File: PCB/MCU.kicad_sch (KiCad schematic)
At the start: 34 parts, among them J1 SWD, Q1 AO3400A, SW32 USB Boot, SW33 Reset, U2 W25Q128JVS, U3 RP2040, Y1 12MHz

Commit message: More routing
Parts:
- J1: now not fitted
- SW32: footprint Cantaloupe:SW_DIP_SPSTx01_Slide_6.7x4.1mm_W8.61mm_P2.54mm_LowProfile-Dual -> Cantaloupe:SW_DIP_SPSTx01_Slide_6.7x4.1mm_W8.61mm_P2.54mm_LowProfile-Flippable
- SW33: footprint Cantaloupe:SW_SPST_TL3342-Dual -> Cantaloupe:SW_SPST_TL3342-Flippable
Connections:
- net ROTA: now also U3.28 (GPIO17); no longer U3.27 (GPIO16)
- net ROTB: now also U3.29 (GPIO18); no longer U3.28 (GPIO17)
- net ROW4: now also U3.27 (GPIO16); no longer U3.29 (GPIO18)
- net Side: now also U3.14 (GPIO11)
- net RGB_3V3: now reaches Q1.2 (S), R19.1, U3.34 (GPIO22)
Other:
- moved on the sheet: JP1, JP2, Q1, R10, R19, R20

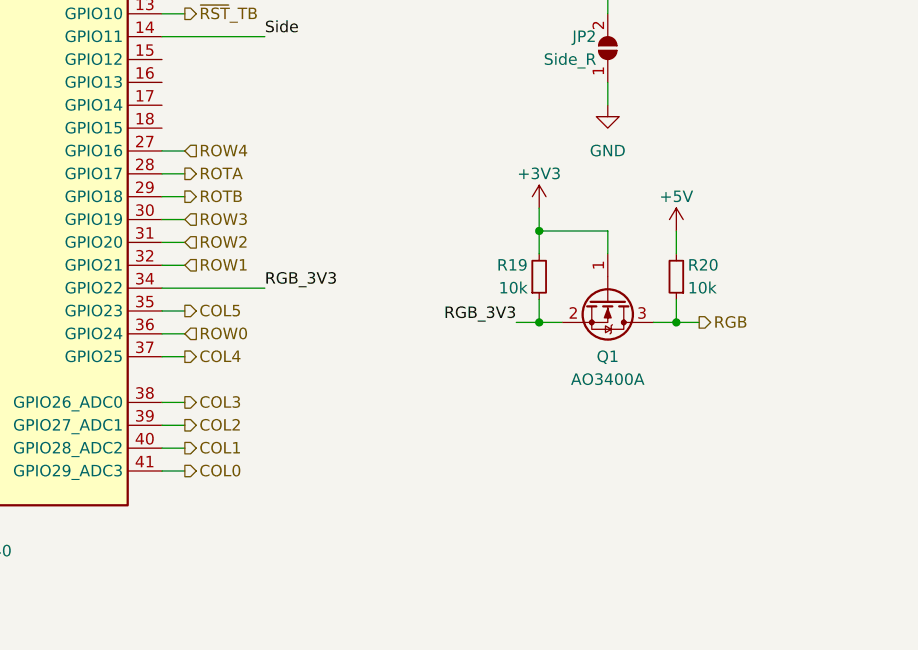
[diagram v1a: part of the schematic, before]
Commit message: Routing done. Ogen footprint added.
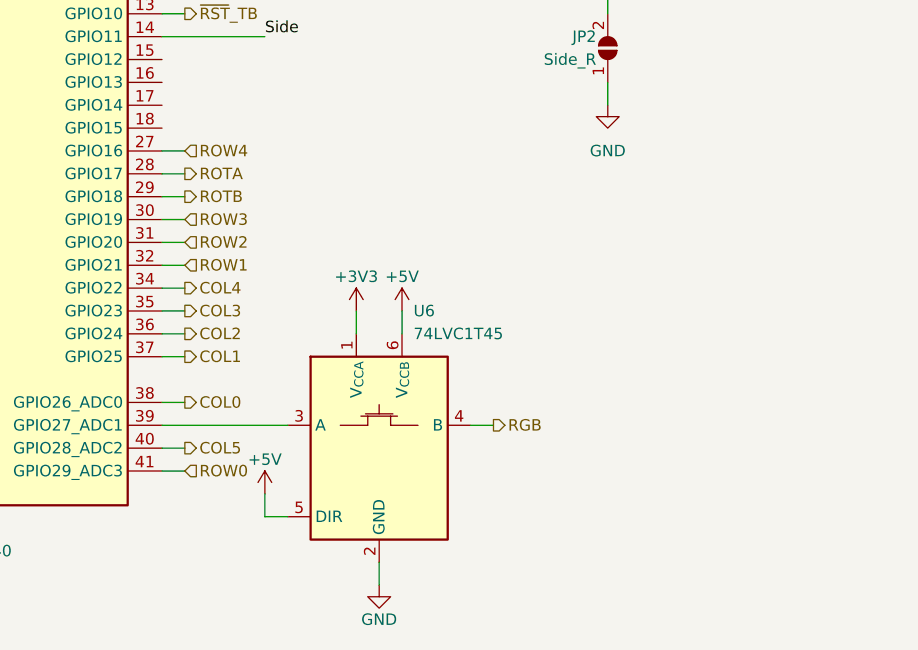
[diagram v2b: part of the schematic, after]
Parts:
- removed Q1: AO3400A, Package_TO_SOT_SMD:SOT-23, symbol Transistor_FET:AO3400A
- removed R19, R20: 10k, Resistor_SMD:R_0402_1005Metric, symbol Device:R_Small
- added U6: 74LVC1T45, Package_TO_SOT_SMD:SOT-363_SC-70-6, symbol Cantaloupe:74LVC1T45
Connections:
- net RGB_3V3 is gone; now on net COL4: U3.34 (GPIO22)
- net +3V3: now also U6.1 (V_{CCA})
- net +5V: now also U6.5 (DIR), U6.6 (V_{CCB})
- net COL0: now also U3.38 (GPIO26_ADC0); no longer U3.41 (GPIO29_ADC3)
- net COL1: now also U3.37 (GPIO25); no longer U3.40 (GPIO28_ADC2)
- net COL2: now also U3.36 (GPIO24); no longer U3.39 (GPIO27_ADC1)
- net COL3: now also U3.35 (GPIO23); no longer U3.38 (GPIO26_ADC0)
- net COL4: no longer U3.37 (GPIO25)
- net COL5: now also U3.40 (GPIO28_ADC2); no longer U3.35 (GPIO23)
- net GND: now also U6.2 (GND)
- net RGB: now also U6.4 (B)
- net ROW0: now also U3.41 (GPIO29_ADC3); no longer U3.36 (GPIO24)
- new net: U3.39 (GPIO27_ADC1), U6.3 (A)

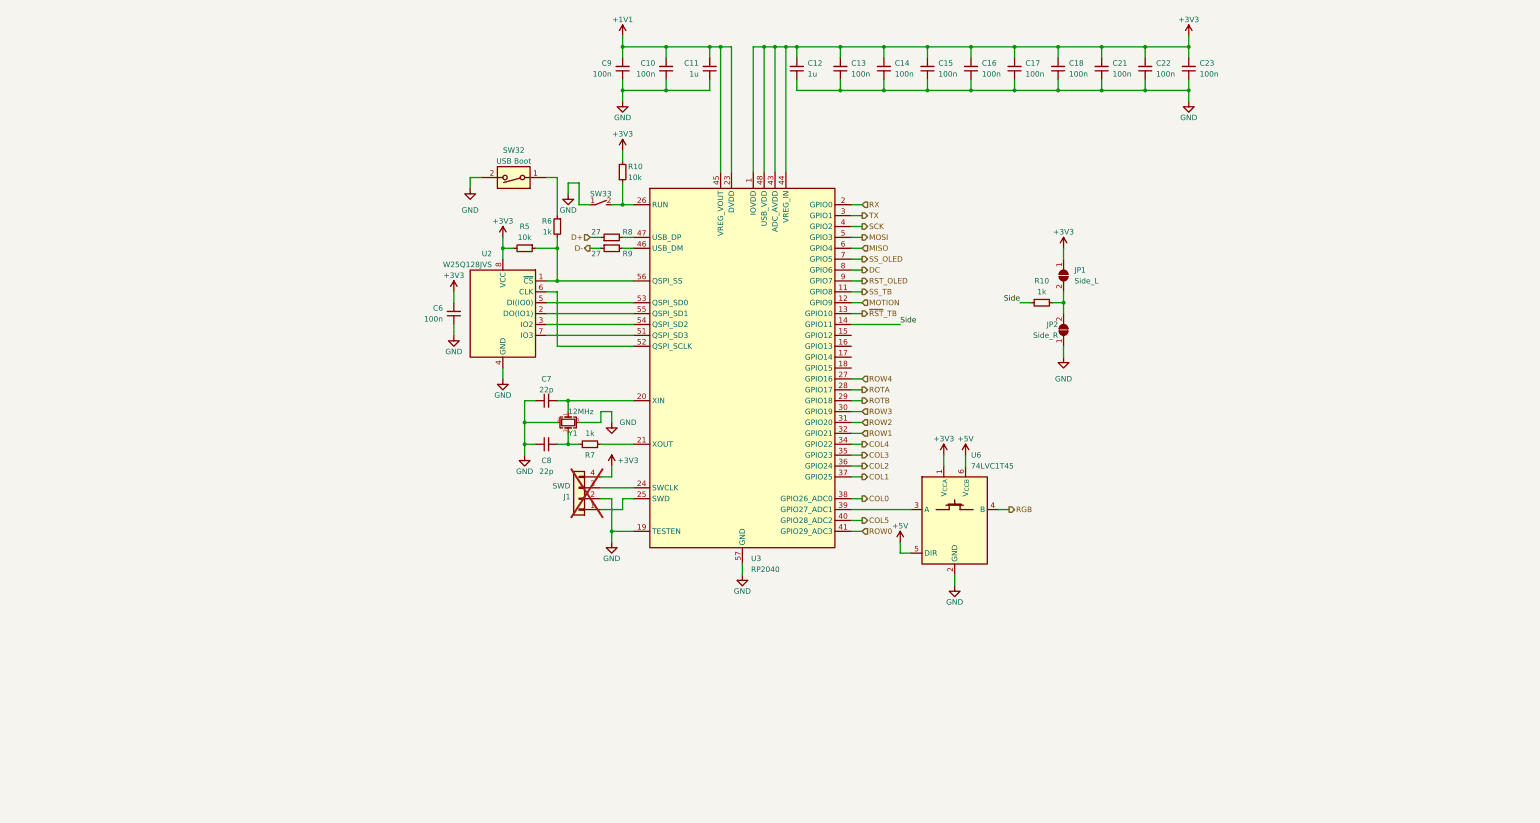
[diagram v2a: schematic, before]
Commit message: 08/08/2023 update
Removed Ogen footprint, and future VIK support is planned. Rerouted board following latest Honeydew revision. WIP support for the USB2541 is added, but it's very tentative and not yet complete. Added CX70M-24P1 footprint.
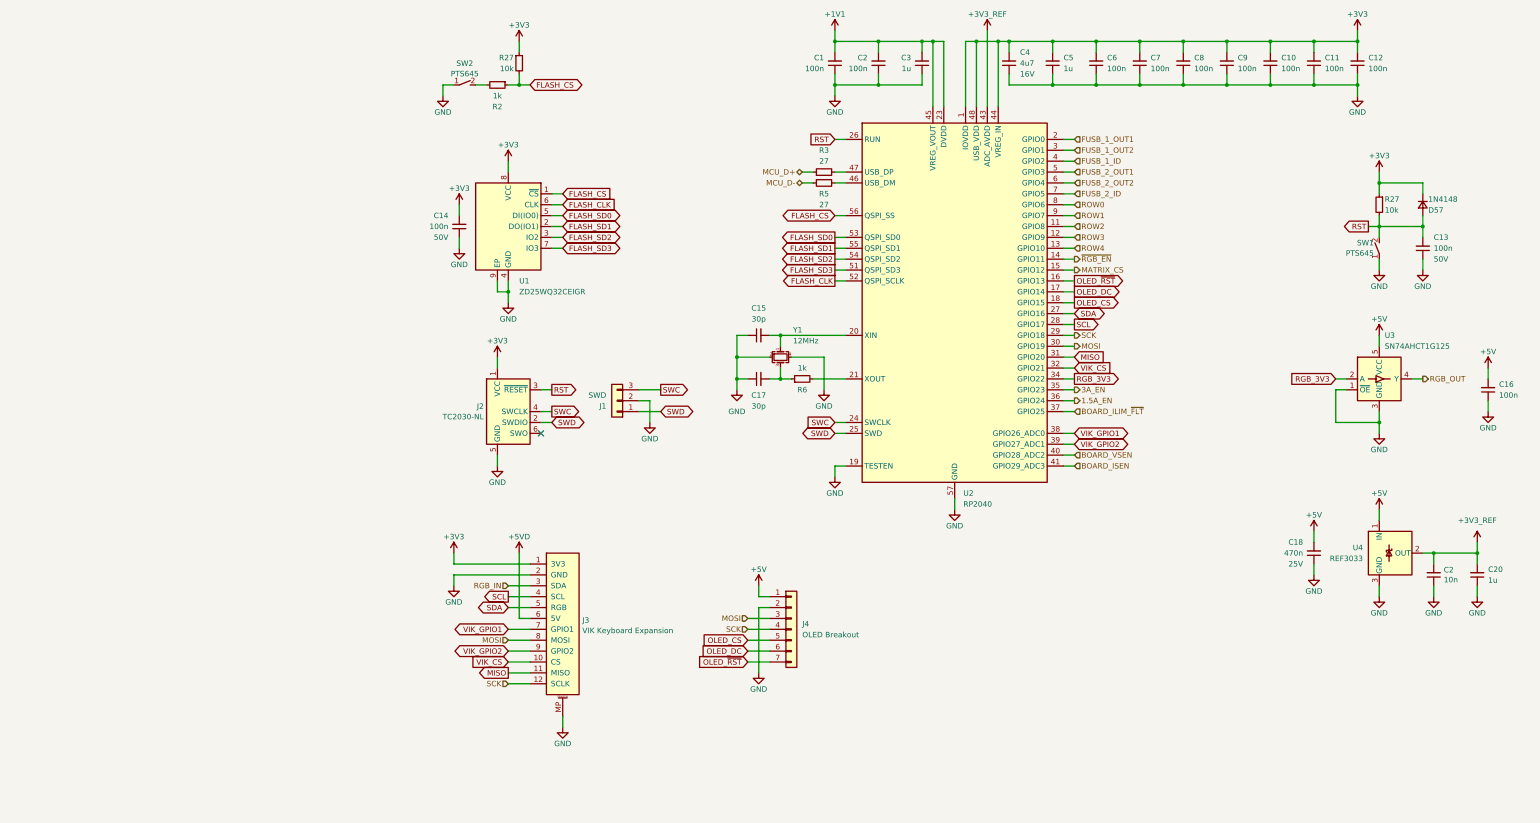
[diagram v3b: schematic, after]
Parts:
- removed C21, C22, C23: 100n, Capacitor_SMD:C_0402_1005Metric, symbol Device:C_Small
- removed J1: SWD, Connector_PinHeader_2.54mm:PinHeader_1x04_P2.54mm_Vertical, symbol Connector_Generic:Conn_01x04
- removed JP1: Side_L, Jumper:SolderJumper-2_P1.3mm_Open_Pad1.0x1.5mm, symbol Jumper:SolderJumper_2_Open
- removed JP2: Side_R, Jumper:SolderJumper-2_P1.3mm_Open_Pad1.0x1.5mm, symbol Jumper:SolderJumper_2_Open
- removed R10, R7: 1k, Resistor_SMD:R_0402_1005Metric, symbol Device:R_Small
- removed R10: 10k, Resistor_SMD:R_0402_1005Metric, symbol Device:R_Small
- removed R8, R9: 27, Resistor_SMD:R_0402_1005Metric, symbol Device:R_Small
- removed SW32: USB Boot, Cantaloupe:SW_DIP_SPSTx01_Slide_6.7x4.1mm_W8.61mm_P2.54mm_LowProfile-Flippable, symbol Switch:SW_DIP_x01
- removed SW33: Reset, Cantaloupe:SW_SPST_TL3342-Flippable, symbol Cantaloupe:SW_SPST_Small
- removed U2: W25Q128JVS, Package_SO:SOIC-8_5.23x5.23mm_P1.27mm, symbol Memory_Flash:W25Q128JVS
- removed U3: RP2040, Cantaloupe:QFN-56-1EP_7x7mm_P0.4mm_EP3.2x3.2mm_ThermalVias, symbol MCU_RaspberryPi:RP2040
- removed U6: 74LVC1T45, Package_TO_SOT_SMD:SOT-363_SC-70-6, symbol Cantaloupe:74LVC1T45
- added C1, C2: 100n, Capacitor_SMD:C_0402_1005Metric, symbol Device:C_Small
- added C2: 10n, Capacitor_SMD:C_0402_1005Metric, symbol Device:C_Small
- added C20, C3, C5: 1u, Capacitor_SMD:C_0402_1005Metric, symbol Device:C_Small
- added C4: 4u7, Capacitor_SMD:C_0603_1608Metric, symbol Device:C_Small
- added D57: 1N4148, Cantaloupe:D_SOD-323, symbol Device:D_Small
- added J1: SWD, Cantaloupe:Header_SWD, symbol Connector_Generic:Conn_01x03
- added J2: TC2030-NL, Connector:Tag-Connect_TC2030-IDC-NL_2x03_P1.27mm_Vertical, symbol Connector:Conn_ARM_SWD_TagConnect_TC2030-NL
- added J3: VIK Keyboard Expansion, Cantaloupe:vik-keyboard-connector-horizontal, symbol Honeydew:vik-keyboard-connector
- added J4: OLED Breakout, Cantaloupe:OLED_1.5_SSD1351_128x128, symbol Connector_Generic:Conn_01x07
- added R2: 1k, Resistor_SMD:R_0402_1005Metric, symbol Device:R_Small
- added R27 (x2): 10k, Resistor_SMD:R_0402_1005Metric, symbol Device:R_Small
- added R3: 27, Resistor_SMD:R_0402_1005Metric, symbol Device:R_Small
- added SW1, SW2: PTS645, Cantaloupe:SW_SPST_PTS645, symbol Cantaloupe:SW_SPST_Small
- added U1: ZD25WQ32CEIGR, Cantaloupe:USON-8-1EP_3x2mm_P0.5mm_EP1.6x0.2mm, symbol Memory_Flash:W25Q32JVZP
- added U2: RP2040, Cantaloupe:QFN-56-1EP_7x7mm_P0.4mm_EP3.2x3.2mm_ThermalVias, symbol MCU_RaspberryPi:RP2040
- added U3: SN74AHCT1G125, Package_TO_SOT_SMD:SOT-353_SC-70-5, symbol Honeydew:SN74AHCT1G125
- added U4: REF3033, Cantaloupe:SOT-23-3, symbol Reference_Voltage:REF3033
- C10, C13, C14, C16, C6, C9: LCSC C1525 -> C307331; Voltage (none) -> 50V
- C11, C12: value 1u -> 100n; footprint Capacitor_SMD:C_0603_1608Metric -> Capacitor_SMD:C_0402_1005Metric; LCSC C15849 -> C307331; Voltage (none) -> 50V
- C15, C17: value 100n -> 30p; LCSC C1525 -> C1570; Voltage (none) -> 50V
- C18: value 100n -> 470n; footprint Capacitor_SMD:C_0402_1005Metric -> Capacitor_SMD:C_0603_1608Metric; LCSC C1525 -> C1623; Voltage (none) -> 25V
- C7, C8: value 22p -> 100n; LCSC C1555 -> C307331; Voltage (none) -> 50V
- R5: value 10k -> 27; LCSC C25744 -> C25100; now in the parts list
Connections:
- net +1V1: now also C1.2, C2.2, C3.2, U2.23 (DVDD), U2.45 (VREG_VOUT), U2.50 (DVDD); no longer C10.2, C11.2, C9.2
- net +3V3: now also C10.2, C11.2, C7.2, C8.2, C9.2, C4.2, C5.2, D57.1 (K), J2.1 (VCC), J3.1 (3V3), R27.1, R27.1, U1.8 (VCC), U2.1 (IOVDD), U2.10 (IOVDD), U2.22 (IOVDD), U2.33 (IOVDD), U2.42 (IOVDD), U2.44 (VREG_IN), U2.48 (USB_VDD), U2.49 (IOVDD); no longer C13.2, C15.2, C16.2, C17.2, C18.2, R5.2
- net +5V: now also C16.2, C18.2, J4.1 (Pin_1), U3.5 (VCC), U4.1 (IN)
- net GND: now also C1.1, C2.1, C2.1, C20.1, C3.1, C4.1, C5.1, J1.2 (Pin_2), J2.5 (GND), J3.2 (GND), J3.MP, J4.2 (Pin_2), SW1.1 (A), SW2.1 (A), U1.4 (GND), U1.9 (EP), U2.19 (TESTEN), U2.57 (GND), U3.1 (~{OE}), U3.3 (GND), U4.3 (GND)
- net MISO: now also J3.11 (MISO), U2.31 (GPIO20)
- net MOSI: now also J3.8 (MOSI), J4.3 (Pin_3), U2.30 (GPIO19)
- net ROW0: now also U2.8 (GPIO6)
- net ROW1: now also U2.9 (GPIO7)
- net ROW2: now also U2.11 (GPIO8)
- net ROW3: now also U2.12 (GPIO9)
- net ROW4: now also U2.13 (GPIO10)
- net SCK: now also J3.12 (SCLK), J4.4 (Pin_4), U2.29 (GPIO18)
- net at R6.1: now also C17.2, Y1.3
- net at R6.2: now also U2.21 (XOUT); no longer R5.1
- net at Y1.1: now also C15.2, U2.20 (XIN); no longer C7.2
- new net: R3.2, U2.47 (USB_DP)
- new net: R5.2, U2.46 (USB_DM)
- new net: R2.2, SW2.2 (B)
- new net +3V3_REF: C2.2, C20.2, U2.43 (ADC_AVDD), U4.2 (OUT)
- new net +5VD: J3.6 (5V)
- new net 1.5A_EN: U2.36 (GPIO24)
- new net 3A_EN: U2.35 (GPIO23)
- new net BOARD_ILIM_~{FLT}: U2.37 (GPIO25)
- new net BOARD_ISEN: U2.41 (GPIO29_ADC3)
- new net BOARD_VSEN: U2.40 (GPIO28_ADC2)
- new net FLASH_CLK: U1.6 (CLK), U2.52 (QSPI_SCLK)
- new net FLASH_CS: R2.1, R27.2, U1.1 (~{CS}), U2.56 (QSPI_SS)
- new net FLASH_SD0: U1.5 (DI(IO0)), U2.53 (QSPI_SD0)
- new net FLASH_SD1: U1.2 (DO(IO1)), U2.55 (QSPI_SD1)
- new net FLASH_SD2: U1.3 (IO2), U2.54 (QSPI_SD2)
- new net FLASH_SD3: U1.7 (IO3), U2.51 (QSPI_SD3)
- new net FUSB_1_ID: U2.4 (GPIO2)
- new net FUSB_1_OUT1: U2.2 (GPIO0)
- new net FUSB_1_OUT2: U2.3 (GPIO1)
- new net FUSB_2_ID: U2.7 (GPIO5)
- new net FUSB_2_OUT1: U2.5 (GPIO3)
- new net FUSB_2_OUT2: U2.6 (GPIO4)
- new net MATRIX_CS: U2.15 (GPIO12)
- new net MCU_D+: R3.1
- new net MCU_D-: R5.1
- new net OLED_CS: J4.5 (Pin_5), U2.18 (GPIO15)
- new net OLED_DC: J4.6 (Pin_6), U2.17 (GPIO14)
- new net OLED_~{RST}: J4.7 (Pin_7), U2.16 (GPIO13)
- new net RGB_3V3: U2.34 (GPIO22), U3.2 (A)
- new net RGB_IN: J3.3 (SDA)
- new net RGB_OUT: U3.4 (Y)
- new net RST: C13.2, D57.2 (A), J2.3 (~{RESET}), R27.2, SW1.2 (B), U2.26 (RUN)
- new net SCL: J3.4 (SCL), U2.28 (GPIO17)
- new net SDA: J3.5 (RGB), U2.27 (GPIO16)
- new net SWC: J1.3 (Pin_3), J2.4 (SWCLK), U2.24 (SWCLK)
- new net SWD: J1.1 (Pin_1), J2.2 (SWDIO), U2.25 (SWD)
- new net VIK_CS: J3.10 (CS), U2.32 (GPIO21)
- new net VIK_GPIO1: J3.7 (GPIO1), U2.38 (GPIO26_ADC0)
- new net VIK_GPIO2: J3.9 (GPIO2), U2.39 (GPIO27_ADC1)
- new net ~{RGB_EN}: U2.14 (GPIO11)
- no-connect marks 0 -> 1
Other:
- company: (none) -> Created by Ariamelon (https://github.com/Ariamelon/Cantaloupe/)
- title: (none) -> Cantaloupe split ergonomic keyboard
